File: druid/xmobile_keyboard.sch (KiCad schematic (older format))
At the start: 34 parts, among them SW10 SW_PUSH, SW11 SW_PUSH, SW12 SW_PUSH, SW13 SW_PUSH, SW14 SW_PUSH, SW15 SW_PUSH, SW16 SW_PUSH, SW17 SW_PUSH, SW18 SW_PUSH, SW19 SW_PUSH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

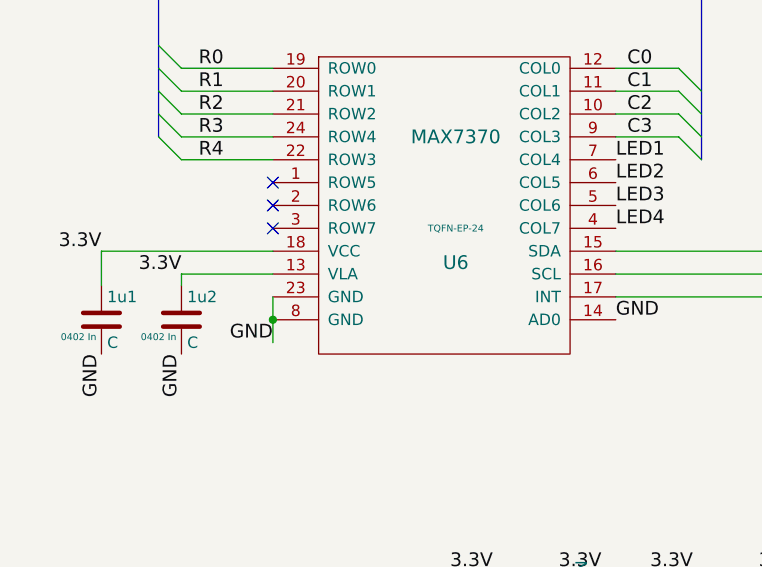
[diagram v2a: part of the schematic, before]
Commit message: KBD controller and SRAM packages changed from BGA to ... TSOP and TQFN XMEGA packaged need to be changed
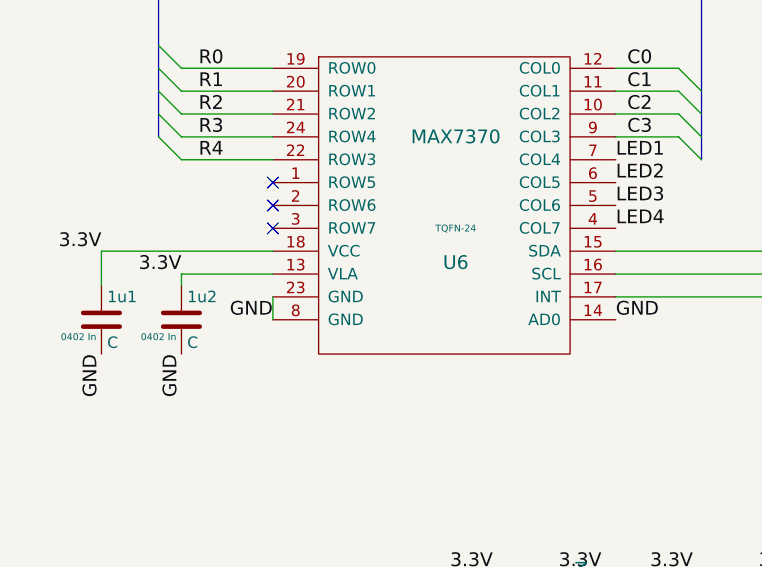
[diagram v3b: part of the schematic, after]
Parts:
- U6: footprint druid:W252F2+1_21-0453 -> Housings_DFN_QFN:QFN-24-1EP_4x4mm_Pitch0.5mm; case TQFN-EP-24 -> TQFN-24
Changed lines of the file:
@@
 F 0 "U6" H 2600 3600 60  0000 C CNN
 F 1 "MAX7370" H 2600 4150 60  0000 C CNN
-F 2 "druid:W252F2+1_21-0453" H 2575 3100 60  0001 C CNN
+F 2 "Housings_DFN_QFN:QFN-24-1EP_4x4mm_Pitch0.5mm" H 2575 3100 60  0001 C CNN
 F 3 "https://eu.mouser.com/datasheet/2/256/MAX7370-1514852.pdf" H 3550 3650 60  0001 C CNN
 F 4 "https://eu.mouser.com/ProductDetail/Maxim-Integrated/MAX7370ETG%2b?qs=sGAEpiMZZMsE420DPIasPtOxRlHUUjJIUcrVTuCuU7c%3d" H 2600 3750 60  0001 C CNN "example"
-F 5 "TQFN-EP-24" H 2600 3750 30  0000 C CNN "case"
+F 5 "TQFN-24" H 2600 3750 30  0000 C CNN "case"
 	1    2600 3750
 	1    0    0    -1
@@
 Text Label 1075 7550 0    60   ~ 0
 GND
-Text Label 1800 4250 2    60   ~ 0
+Text Label 1800 4150 2    60   ~ 0
 GND
 NoConn ~ 1800 3650
@@
 Wire Wire Line
 	1800 4050 1800 4150
-Connection ~ 1800 4150
 Wire Wire Line
 	4300 2550 4600 2550
@@
 	8125 4850 8975 4850
 Wire Wire Line
-	1800 4150 1800 4250
-Wire Wire Line
 	4600 2550 4900 2550

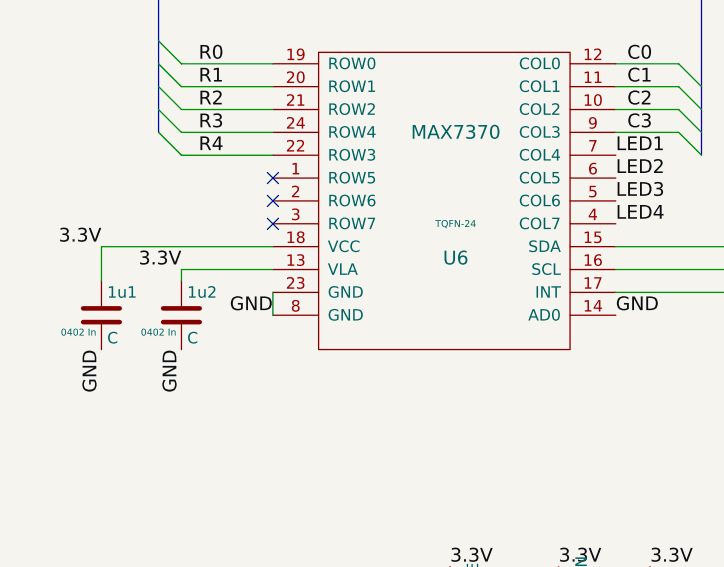
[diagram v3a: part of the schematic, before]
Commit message: Done with packages. Start to place components.
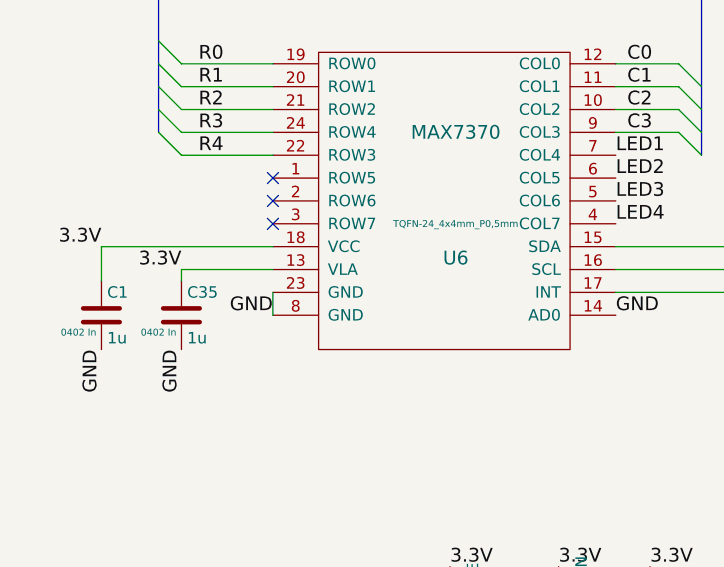
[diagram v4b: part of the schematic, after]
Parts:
- C1: renamed from 1u1; value C -> 1u
- C35: renamed from 1u2; value C -> 1u
- U6: footprint Housings_DFN_QFN:QFN-24-1EP_4x4mm_Pitch0.5mm -> Package_DFN_QFN:QFN-24-1EP_4x4mm_P0.5mm_EP2.7x2.7mm; case TQFN-24 -> TQFN-24_4x4mm_P0,5mm
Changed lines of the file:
@@
 F 0 "U6" H 2600 3600 60  0000 C CNN
 F 1 "MAX7370" H 2600 4150 60  0000 C CNN
-F 2 "Housings_DFN_QFN:QFN-24-1EP_4x4mm_Pitch0.5mm" H 2575 3100 60  0001 C CNN
+F 2 "Package_DFN_QFN:QFN-24-1EP_4x4mm_P0.5mm_EP2.7x2.7mm" H 2575 3100 60  0001 C CNN
 F 3 "https://eu.mouser.com/datasheet/2/256/MAX7370-1514852.pdf" H 3550 3650 60  0001 C CNN
 F 4 "https://eu.mouser.com/ProductDetail/Maxim-Integrated/MAX7370ETG%2b?qs=sGAEpiMZZMsE420DPIasPtOxRlHUUjJIUcrVTuCuU7c%3d" H 2600 3750 60  0001 C CNN "example"
-F 5 "TQFN-24" H 2600 3750 30  0000 C CNN "case"
+F 5 "TQFN-24_4x4mm_P0,5mm" H 2600 3750 30  0000 C CNN "case"
 	1    2600 3750
 	1    0    0    -1
@@
 INT
 $Comp
-L xmobile-rescue:C 1u1
+L xmobile-rescue:C C1
 U 1 1 5C4C0F77
 P 1050 4150
-F 0 "1u1" H 1075 4250 50  0000 L CNN
-F 1 "C" H 1075 4050 50  0000 L CNN
+F 0 "C1" H 1075 4250 50  0000 L CNN
+F 1 "1u" H 1075 4050 50  0000 L CNN
 F 2 "Capacitor_SMD:C_0402_1005Metric" H 1088 4000 50  0001 C CNN
 F 3 "https://eu.mouser.com/datasheet/2/281/murata_03052018_GRM_Series_1-1310166.pdf" H 1050 4150 50  0001 C CNN
@@
 $EndComp
 $Comp
-L xmobile-rescue:C 1u2
+L xmobile-rescue:C C35
 U 1 1 5C6E6190
 P 1400 4150
-F 0 "1u2" H 1425 4250 50  0000 L CNN
-F 1 "C" H 1425 4050 50  0000 L CNN
+F 0 "C35" H 1425 4250 50  0000 L CNN
+F 1 "1u" H 1425 4050 50  0000 L CNN
 F 2 "Capacitor_SMD:C_0402_1005Metric" H 1438 4000 50  0001 C CNN
 F 3 "https://eu.mouser.com/datasheet/2/281/murata_03052018_GRM_Series_1-1310166.pdf" H 1400 4150 50  0001 C CNN
